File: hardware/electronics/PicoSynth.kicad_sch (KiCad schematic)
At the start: 29 parts, among them U1 Pico, U2 PCM5102A, U3 TC1262-33, U4 TC1262-33

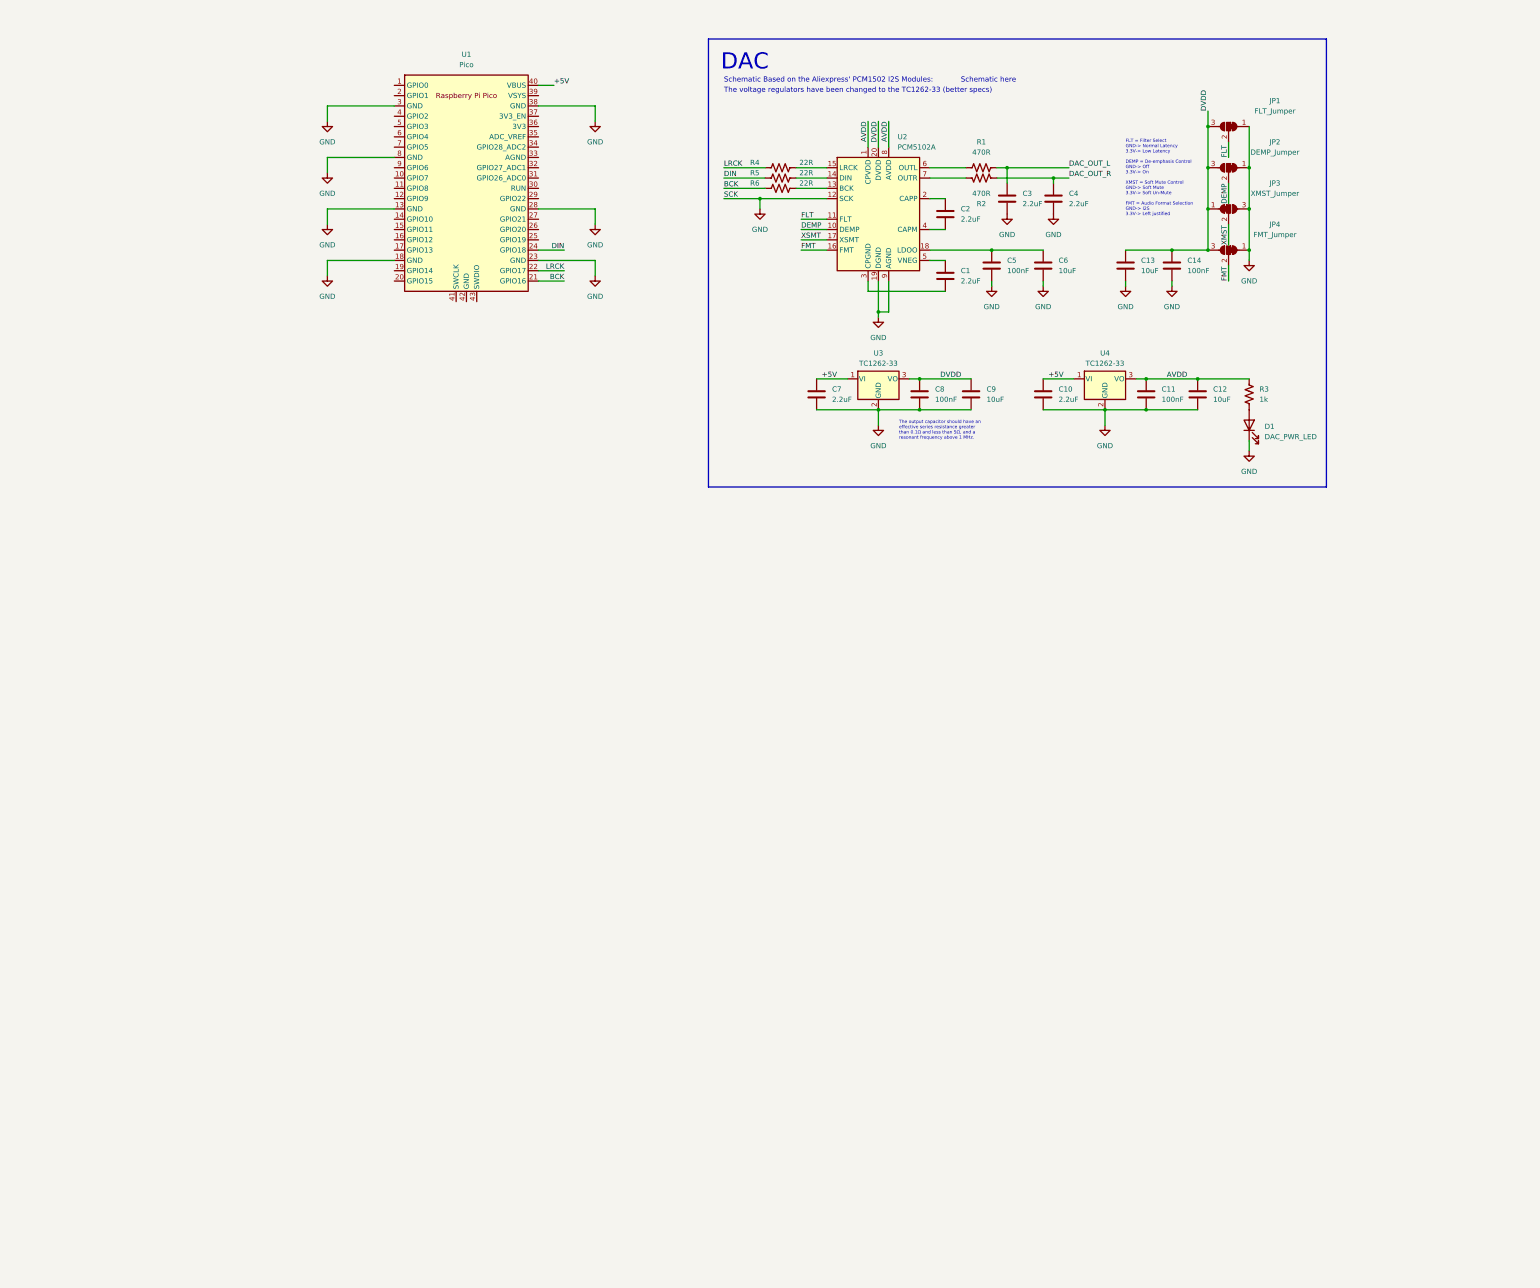
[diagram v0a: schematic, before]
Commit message: A lot of updates in the Schematic... To-Do: hot swaps in switches, SD card and I2C for screen
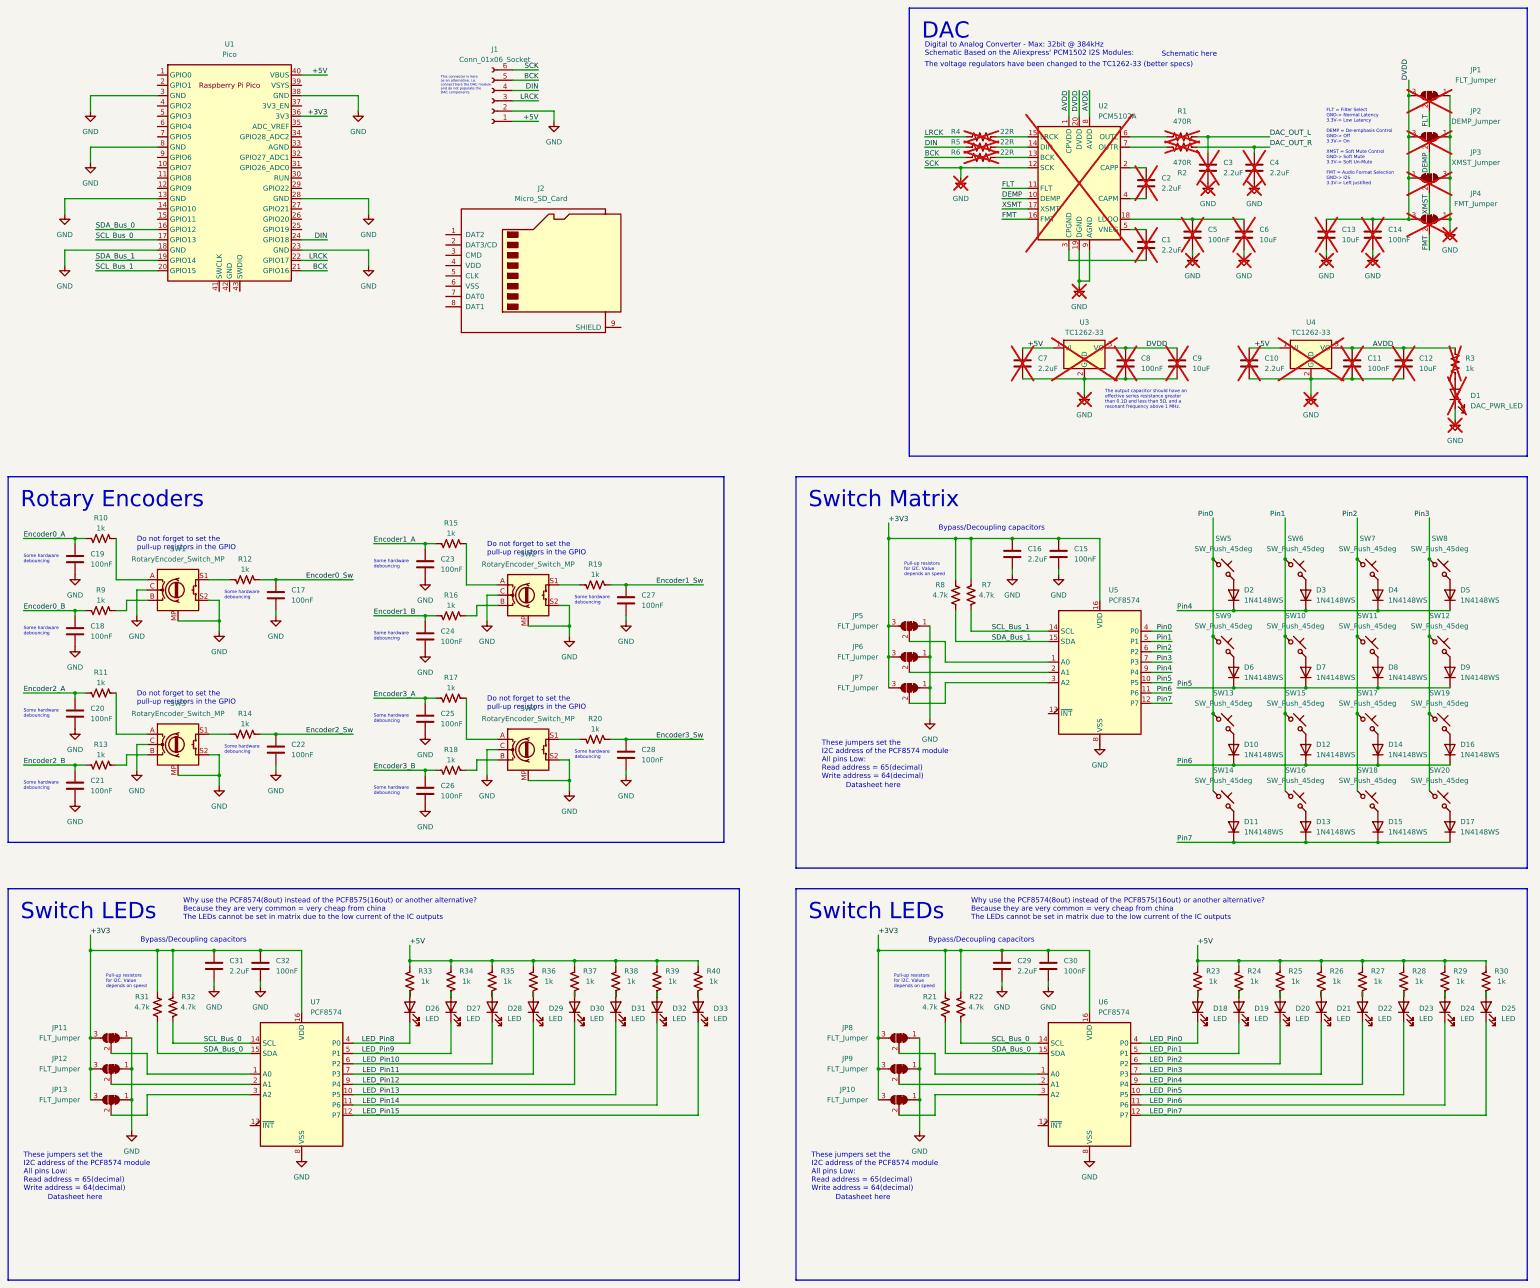
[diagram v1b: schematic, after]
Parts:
- added C15, C17, C18, C19, C20, C21, C22, C23, C24, C25, C26, C27, C28, C30, C32: 100nF, Cern_Ignition:C_0805_2012Metric_Pad1.18x1.45mm_HandSolder_modif, symbol Device:C
- added C16, C29, C31: 2.2uF, Cern_Ignition:C_0805_2012Metric_Pad1.18x1.45mm_HandSolder_modif, symbol Device:C
- added D10, D11, D12, D13, D14, D15, D16, D17, D2, D3, D4, D5, D6, D7, D8, D9: 1N4148WS, Diode_SMD:D_SOD-323, symbol Diode:1N4148WS
- added D18, D19, D20, D21, D22, D23, D24, D25, D26, D27, D28, D29, D30, D31, D32, D33: LED, symbol Device:LED
- added J1: Conn_01x06_Socket, Connector_PinSocket_2.54mm:PinSocket_1x06_P2.54mm_Vertical, symbol Connector:Conn_01x06_Socket
- added J2: Micro_SD_Card, symbol Connector:Micro_SD_Card
- added JP10, JP11, JP12, JP13, JP5, JP6, JP7, JP8, JP9: FLT_Jumper, Jumper:SolderJumper-3_P1.3mm_Open_RoundedPad1.0x1.5mm_NumberLabels, symbol Jumper:SolderJumper_3_Bridged12
- added R10, R11, R12, R13, R14, R15, R16, R17, R18, R19, R20, R23, R24, R25, R26, R27, R28, R29, R30, R33, R34, R35, R36, R37, R38, R39, R40, R9: 1k, Cern_Ignition:R_0805_2012Metric_Pad1.20x1.40mm_HandSolder_modif, symbol Device:R_US
- added R21, R22, R31, R32, R7, R8: 4.7k, Cern_Ignition:R_0805_2012Metric_Pad1.20x1.40mm_HandSolder_modif, symbol Device:R_US
- added SW1, SW2, SW3, SW4: RotaryEncoder_Switch_MP, Rotary_Encoder:RotaryEncoder_Alps_EC11E-Switch_Vertical_H20mm_CircularMountingHoles, symbol Device:RotaryEncoder_Switch_MP
- added SW10, SW11, SW12, SW13, SW14, SW15, SW16, SW17, SW18, SW19, SW20, SW5, SW6, SW7, SW8, SW9: SW_Push_45deg, Lame_Lib:SW_Cherry_MX_1.00u_PCB, symbol Switch:SW_Push_45deg
- added U5, U6, U7: PCF8574, Package_SO:SOIC-16W_7.5x10.3mm_P1.27mm, symbol Interface_Expansion:PCF8574
- C1, C10, C11, C12, C13, C14, C2, C3, C4, C5, C6, C7, C8, C9, D1, JP1, JP2, JP3, JP4, R1, R2, R3, R4, R5, R6, U2, U3, U4: now not fitted
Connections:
- net +5V: now also J1.1 (Pin_1), R23.1, R24.1, R25.1, R26.1, R27.1, R28.1, R29.1, R30.1, R33.1, R34.1, R35.1, R36.1, R37.1, R38.1, R39.1, R40.1
- net BCK: now also J1.5 (Pin_5)
- net DIN: now also J1.4 (Pin_4)
- net GND: now also C15.2, C16.2, C17.2, C18.2, C19.2, C20.2, C21.2, C22.2, C23.2, C24.2, C25.2, C26.2, C27.2, C28.2, C29.2, C30.2, C31.2, C32.2, J1.2 (Pin_2), J1.6 (Pin_6), JP10.1 (A), JP11.1 (A), JP12.1 (A), JP13.1 (A), JP5.1 (A), JP6.1 (A), JP7.1 (A), JP8.1 (A), JP9.1 (A), SW1.C, SW1.MP, SW1.S2, SW2.C, SW2.MP, SW2.S2, SW3.C, SW3.MP, SW3.S2, SW4.C, SW4.MP, SW4.S2, U5.8 (VSS), U6.8 (VSS), U7.8 (VSS)
- net LRCK: now also J1.3 (Pin_3)
- net SDA_Bus_0: now reaches U1.16 (GPIO12)
- net SDA_Bus_0: now also R21.2, R31.2, U6.15 (SDA), U7.15 (SDA)
- net SCL_Bus_0: now reaches U1.17 (GPIO13)
- net SCL_Bus_0: now also R22.2, R32.2, U6.14 (SCL), U7.14 (SCL)
- net SDA_Bus_1: now reaches U1.19 (GPIO14)
- net SDA_Bus_1: now also R8.2, U5.15 (SDA)
- net SCL_Bus_1: now reaches U1.20 (GPIO15)
- net SCL_Bus_1: now also R7.2, U5.14 (SCL)
- net +3V3: now reaches U1.36 (3V3)
- net +3V3: now also C15.1, C16.1, C29.1, C30.1, C31.1, C32.1, JP10.3 (B), JP11.3 (B), JP12.3 (B), JP13.3 (B), JP5.3 (B), JP6.3 (B), JP7.3 (B), JP8.3 (B), JP9.3 (B), R21.1, R22.1, R31.1, R32.1, R7.1, R8.1, U5.16 (VDD), U6.16 (VDD), U7.16 (VDD)
- new net: D8.2 (A), SW11.2
- new net: JP8.2 (C), U6.1 (A0)
- new net: JP9.2 (C), U6.2 (A1)
- new net: JP10.2 (C), U6.3 (A2)
- new net: D21.2 (A), R26.2
- new net: D22.2 (A), R27.2
- new net: D25.2 (A), R30.2
- new net: D14.2 (A), SW17.2
- new net: R14.1, SW3.S1
- new net: R20.1, SW4.S1
- new net: R10.2, SW1.A
- new net: R9.2, SW1.B
- new net: R12.1, SW1.S1
- new net: JP11.2 (C), U7.1 (A0)
- new net: JP12.2 (C), U7.2 (A1)
- new net: JP13.2 (C), U7.3 (A2)
- new net: D29.2 (A), R36.2
- new net: D18.2 (A), R23.2
- new net: R15.2, SW2.A
- new net: D3.2 (A), SW6.2
- new net: R16.2, SW2.B
- new net: D4.2 (A), SW7.2
- new net: D7.2 (A), SW10.2
- new net: D24.2 (A), R29.2
- new net: D27.2 (A), R34.2
- new net: D19.2 (A), R24.2
- new net: D15.2 (A), SW18.2
- new net: R19.1, SW2.S1
- new net: D9.2 (A), SW12.2
- new net: D12.2 (A), SW15.2
- new net: D2.2 (A), SW5.2
- new net: D5.2 (A), SW8.2
- new net: D33.2 (A), R40.2
- new net: D20.2 (A), R25.2
- new net: D16.2 (A), SW19.2
- new net: D23.2 (A), R28.2
- new net: D13.2 (A), SW16.2
- new net: D26.2 (A), R33.2
- new net: JP6.2 (C), U5.2 (A1)
- new net: D11.2 (A), SW14.2
- new net: D17.2 (A), SW20.2
- new net: R13.2, SW3.B
- new net: R18.2, SW4.B
- new net: R11.2, SW3.A
- new net: D31.2 (A), R38.2
- new net: R17.2, SW4.A
- new net: D32.2 (A), R39.2
- new net: D30.2 (A), R37.2
- new net: D10.2 (A), SW13.2
- new net: D28.2 (A), R35.2
- new net: D6.2 (A), SW9.2
- new net: JP5.2 (C), U5.1 (A0)
- new net: JP7.2 (C), U5.3 (A2)
- new net Encoder0_A: C19.1, R10.1
- new net Encoder0_B: C18.1, R9.1
- new net Encoder0_Sw: C17.1, R12.2
- new net Encoder1_A: C23.1, R15.1
- new net Encoder1_B: C24.1, R16.1
- new net Encoder1_Sw: C27.1, R19.2
- new net Encoder2_A: C20.1, R11.1
- new net Encoder2_B: C21.1, R13.1
- new net Encoder2_Sw: C22.1, R14.2
- new net Encoder3_A: C25.1, R17.1
- new net Encoder3_B: C26.1, R18.1
- new net Encoder3_Sw: C28.1, R20.2
- new net LED_Pin0: D18.1 (K), U6.4 (P0)
- new net LED_Pin1: D19.1 (K), U6.5 (P1)
- new net LED_Pin10: D28.1 (K), U7.6 (P2)
- new net LED_Pin11: D29.1 (K), U7.7 (P3)
- new net LED_Pin12: D30.1 (K), U7.9 (P4)
- new net LED_Pin13: D31.1 (K), U7.10 (P5)
- new net LED_Pin14: D32.1 (K), U7.11 (P6)
- new net LED_Pin15: D33.1 (K), U7.12 (P7)
- new net LED_Pin2: D20.1 (K), U6.6 (P2)
- new net LED_Pin3: D21.1 (K), U6.7 (P3)
- new net LED_Pin4: D22.1 (K), U6.9 (P4)
- new net LED_Pin5: D23.1 (K), U6.10 (P5)
- new net LED_Pin6: D24.1 (K), U6.11 (P6)
- new net LED_Pin7: D25.1 (K), U6.12 (P7)
- new net LED_Pin8: D26.1 (K), U7.4 (P0)
- new net LED_Pin9: D27.1 (K), U7.5 (P1)
- new net Pin0: SW13.1, SW14.1, SW5.1, SW9.1, U5.4 (P0)
- new net Pin1: SW10.1, SW15.1, SW16.1, SW6.1, U5.5 (P1)
- new net Pin2: SW11.1, SW17.1, SW18.1, SW7.1, U5.6 (P2)
- new net Pin3: SW12.1, SW19.1, SW20.1, SW8.1, U5.7 (P3)
- new net Pin4: D2.1 (K), D3.1 (K), D4.1 (K), D5.1 (K), U5.9 (P4)
- new net Pin5: D6.1 (K), D7.1 (K), D8.1 (K), D9.1 (K), U5.10 (P5)
- new net Pin6: D10.1 (K), D12.1 (K), D14.1 (K), D16.1 (K), U5.11 (P6)
- new net Pin7: D11.1 (K), D13.1 (K), D15.1 (K), D17.1 (K), U5.12 (P7)
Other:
- note added: "Bypass/Decoupling capacitors"
- note added: "Datasheet here"
- note added: "Digital to Analog Converter - Max: 32bit @ 384kHz Schematic Based on the Aliexpress' PCM1502 I2S Modules:"
- note added: "Do not forget to set the pull-up resistors in the GPIO"
- note added: "Pull-up resistors for I2C. Value depends on speed"
- note added: "Some hardware debouncing"
- note added: "These jumpers set the I2C address of the PCF8574 module All pins Low: Read address = 65(decimal) Write address = 64(decimal)"
- note added: "This connector is here as an alternative, i.e. connect here the DAC module and do not populate the DAC components"
- note added: "Why use the PCF8574(8out) instead of the PCF8575(16out) or another alternative? Because they are very common = very cheap from china The LEDs cannot be set in matrix due to the low current of the IC outputs"
- note removed: "Schematic Based on the Aliexpress' PCM1502 I2S Modules:"
- moved on the sheet: U1

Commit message: SD card and i2c for display added, starting some component placement
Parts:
- added C33: 2.2uF, Cern_Ignition:C_0805_2012Metric_Pad1.18x1.45mm_HandSolder_modif, symbol Device:C
- added C34: 100nF, Cern_Ignition:C_0805_2012Metric_Pad1.18x1.45mm_HandSolder_modif, symbol Device:C
- added J3: Conn_01x04_Socket, Connector_PinSocket_2.54mm:PinSocket_1x04_P2.54mm_Vertical, symbol Connector:Conn_01x04_Socket
- added R41, R42, R43, R44: 10k, Cern_Ignition:R_0805_2012Metric_Pad1.20x1.40mm_HandSolder_modif, symbol Device:R_US
- D10, D11, D12, D13, D14, D15, D16, D17, D2, D3, D4, D5, D6, D7, D8, D9: footprint Diode_SMD:D_SOD-323 -> Diode_SMD:D_0805_2012Metric
- D18, D19, D20, D21, D22, D23, D24, D25, D26, D27, D28, D29, D30, D31, D32, D33: footprint (none) -> LED_SMD:LED_1206_3216Metric
- JP10, JP13, JP7: value FLT_Jumper -> A2_Jumper
- JP11, JP5, JP8: value FLT_Jumper -> A0_Jumper
- JP12, JP6, JP9: value FLT_Jumper -> A1_Jumper
- SW10, SW11, SW12, SW13, SW14, SW15, SW16, SW17, SW18, SW19, SW20, SW5, SW6, SW7, SW8, SW9: footprint Lame_Lib:SW_Cherry_MX_1.00u_PCB -> Cherry_MX_switches:Cherry-MX_PCB-Mounted
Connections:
- net +3V3: now also J2.4 (VDD), C33.1, C34.1, J3.2 (Pin_2), R41.1, R42.1, R43.1, R44.1
- net Encoder0_A: now also U1.9 (GPIO6)
- net Encoder0_B: now also U1.10 (GPIO7)
- net Encoder0_Sw: now also U1.11 (GPIO8)
- net Encoder1_A: now also U1.14 (GPIO10)
- net Encoder1_B: now also U1.15 (GPIO11)
- net Encoder1_Sw: now also U1.12 (GPIO9)
- net Encoder2_A: now also U1.27 (GPIO21)
- net Encoder2_B: now also U1.26 (GPIO20)
- net Encoder2_Sw: now also U1.25 (GPIO19)
- net Encoder3_A: now also U1.31 (GPIO26_ADC0)
- net Encoder3_B: now also U1.30 (RUN)
- net Encoder3_Sw: now also U1.29 (GPIO22)
- net GND: now also J2.6 (VSS), C33.2, C34.2, J3.1 (Pin_1)
- net SCL_Bus_0: now also J3.3 (Pin_3)
- net SDA_Bus_0: now also J3.4 (Pin_4)
- net CD: now reaches J2.2 (DAT3/CD)
- net CD: now also U1.7 (GPIO5), R41.2
- net CMD: now reaches J2.3 (CMD)
- net CMD: now also U1.5 (GPIO3), R42.2
- net CLK: now reaches J2.5 (CLK)
- net CLK: now also U1.4 (GPIO2), R43.2
- net DAT0: now reaches J2.7 (DAT0)
- net DAT0: now also U1.6 (GPIO4), R44.2
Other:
- note added: "Decoupling Caps"
- note added: "Maybe we do not need these resistors if we use internal pull-up"
- moved on the sheet: J1, J2, U1

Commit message: New horizontal layout
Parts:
- added J4: Conn_01x09_Socket, Connector_PinSocket_2.54mm:PinSocket_1x09_P2.54mm_Vertical, symbol Connector:Conn_01x09_Socket
- D10, D11, D12, D13, D14, D15, D16, D17, D2, D3, D4, D5, D6, D7, D8, D9: footprint Diode_SMD:D_0805_2012Metric -> Diode_SMD:D_0805_2012Metric_Pad1.15x1.40mm_HandSolder
- D18, D19, D20, D21, D22, D23, D24, D25, D26, D27, D28, D29, D30, D31, D32, D33: footprint LED_SMD:LED_1206_3216Metric -> LED_SMD:LED_1210_3225Metric_Pad1.42x2.65mm_HandSolder
- SW1, SW2, SW3, SW4: footprint Rotary_Encoder:RotaryEncoder_Alps_EC11E-Switch_Vertical_H20mm_CircularMountingHoles -> Lame_Lib:RotaryEncoder_Alps_EC11E-Switch_Vertical_H20mm_CircularMountingHoles
- SW10, SW11, SW12, SW13, SW14, SW15, SW16, SW17, SW18, SW19, SW20, SW5, SW6, SW7, SW8, SW9: footprint Cherry_MX_switches:Cherry-MX_PCB-Mounted -> Cherry_MX_switches:Cherry-MX_PCB-Mounted_LTST-A683CEGBW_Kailh_Socket
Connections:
- net +5V: now also J1.6 (Pin_6); no longer J1.1 (Pin_1)
- net BCK: now also J1.2 (Pin_2); no longer J1.5 (Pin_5)
- net DIN: now also J1.3 (Pin_3); no longer J1.4 (Pin_4)
- net GND: now also J1.1 (Pin_1), J1.5 (Pin_5); no longer J1.2 (Pin_2), J1.6 (Pin_6)
- net LRCK: now also J1.4 (Pin_4); no longer J1.3 (Pin_3)
- new net 1: J4.9 (Pin_9)
- new net 2: J4.8 (Pin_8)
- new net 3: J4.7 (Pin_7)
- new net 4: J4.6 (Pin_6)
- new net 5: J4.5 (Pin_5)
- new net G: J4.2 (Pin_2), J4.4 (Pin_4)
- new net L: J4.1 (Pin_1)
- new net R: J4.3 (Pin_3)
- no-connect marks 0 -> 8
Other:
- moved on the sheet: C1, C10, C11, C12, C13, C14, C2, C3, C33, C34, C4, C5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

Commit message: This layout could work, need to ponder
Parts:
- added C35: 2.2uF, Cern_Ignition:C_0805_2012Metric_Pad1.18x1.45mm_HandSolder_modif, symbol Device:C
- added C36: 100nF, Cern_Ignition:C_0805_2012Metric_Pad1.18x1.45mm_HandSolder_modif, symbol Device:C
- added C37: 10uF, Cern_Ignition:C_1206_3216Metric_Pad1.33x1.80mm_HandSolder_modif, symbol Device:C
- added JP14: A2_Jumper, Jumper:SolderJumper-3_P1.3mm_Open_RoundedPad1.0x1.5mm_NumberLabels, symbol Jumper:SolderJumper_3_Bridged12
- added U8: AMS1117-3.3, Package_TO_SOT_SMD:SOT-223-3_TabPin2, symbol Regulator_Linear:AMS1117-3.3
- SW10, SW11, SW12, SW13, SW14, SW15, SW16, SW17, SW18, SW19, SW20, SW5, SW6, SW7, SW8, SW9: footprint Cherry_MX_switches:Cherry-MX_PCB-Mounted_LTST-A683CEGBW_Kailh_Socket -> Cherry_MX_switches:Cherry-MX_PCB-Mounted_LTST-A683CEGBW_Kailh_Socket_modif
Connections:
- net +3V3: now also JP11.1 (A), JP14.2 (C); no longer J3.2 (Pin_2), JP11.3 (B), U1.36 (3V3)
- net +5V: now also J3.2 (Pin_2), C35.1, U8.3 (VI)
- net CD: no longer U1.7 (GPIO5)
- net CLK: no longer U1.4 (GPIO2)
- net CMD: no longer U1.5 (GPIO3)
- net DAT0: no longer U1.6 (GPIO4)
- net Encoder0_A: now also U1.14 (GPIO10); no longer U1.9 (GPIO6)
- net Encoder0_B: now also U1.15 (GPIO11); no longer U1.10 (GPIO7)
- net Encoder0_Sw: now also U1.12 (GPIO9); no longer U1.11 (GPIO8)
- net Encoder1_A: now also U1.10 (GPIO7); no longer U1.14 (GPIO10)
- net Encoder1_B: now also U1.11 (GPIO8); no longer U1.15 (GPIO11)
- net Encoder1_Sw: now also U1.9 (GPIO6); no longer U1.12 (GPIO9)
- net Encoder2_A: now also U1.6 (GPIO4); no longer U1.27 (GPIO21)
- net Encoder2_B: now also U1.7 (GPIO5); no longer U1.26 (GPIO20)
- net Encoder2_Sw: now also U1.5 (GPIO3); no longer U1.25 (GPIO19)
- net Encoder3_A: now also U1.2 (GPIO1); no longer U1.31 (GPIO26_ADC0)
- net Encoder3_B: now also U1.4 (GPIO2); no longer U1.30 (RUN)
- net Encoder3_Sw: now also U1.1 (GPIO0); no longer U1.29 (GPIO22)
- net GND: now also JP11.3 (B), C35.2, C36.2, C37.2, U8.1 (GND); no longer JP11.1 (A)
- net SCL_Bus_0: no longer U1.17 (GPIO13)
- net SCL_Bus_1: no longer U1.20 (GPIO15)
- net SDA_Bus_0: no longer U1.16 (GPIO12)
- net SDA_Bus_1: no longer U1.19 (GPIO14)
- net Switch_Interrupt: now reaches U5.13 (~{INT})
- new net +3V3_Pico: JP14.3 (B), U1.36 (3V3)
- new net +3V3_Regulator: C36.1, C37.1, JP14.1 (A), U8.2 (VO)
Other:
- note added: "Headphone amp pam8403D maybe?"
- note added: "Pull-up resistors for I2C. Value depends on speed Do not populate if connecting the oled screen"
- note added: "SSD1306 OLED Module has 10k pull-up in I2C pins"
- note added: "These jumpers set the I2C address of the PCF8574 module All pins Low, A0 HIGH: Read address = 67(decimal) Write address = 66(decimal)"
